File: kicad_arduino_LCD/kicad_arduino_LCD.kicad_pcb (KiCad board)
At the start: 2 copper layers, 68.6 x 53.3 mm, 155 parts, among them P1 Power, P2 Analog, P3 Digital, P4 Digital, P5 CONN_01X01, P6 CONN_01X01, P7 CONN_01X01, P8 CONN_01X01, SW1 SW_Push_Dual_x2, SW2 SW_Push_Dual_x2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

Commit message: Arduino用シールド基板（LCD&RTCモジュール）
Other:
- board text added: "Arduino Clock"

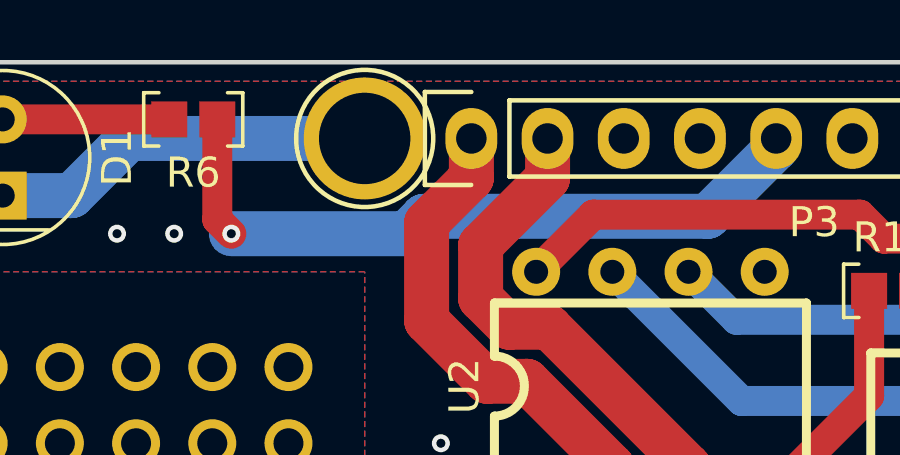
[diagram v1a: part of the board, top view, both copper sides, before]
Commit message: パッドと重なったシルクを削除、Designed by T.kiriya のシルクを追加
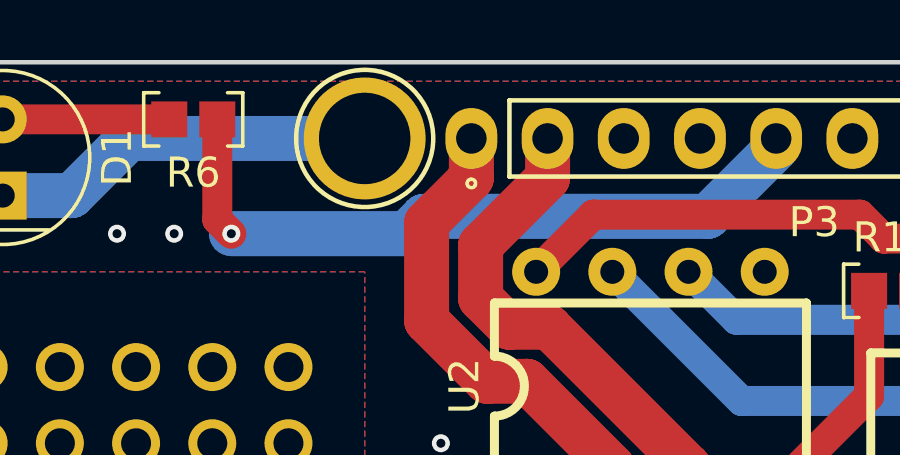
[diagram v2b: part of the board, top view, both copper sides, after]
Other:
- board text added: "Designed by T.kiriya"
